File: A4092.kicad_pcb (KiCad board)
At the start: 2 copper layers, 192.7 x 123.3 mm, 102 parts, among them CN1 Zorro3, J1 Conn_02x25_Odd_Even, J2 Conn_01x06_Pin, J3 TO-LED, J4 TO-MB, J5 5787170-5, J6 350543-1, J7 22112042, SW1 219-8MST, U1 SN74ABT16543DGGR, U10 SN74F244DB, U11 SN74ABT16374ADGGR, U12 74LVC07APW_118, U13 SN74ABT16245ADGGR, U14 74ACT521MTCX, U2 SN74ABT16543DGGR, U3 SN74ABT16543DGGR, U4 NCR53c710 SCSI Host Controller, U5 CY74FCT543ATQCT, U6 ATF1508AS-10AU100, U7 SST39SF010, U8 DS21S07A, U9 DS21S07A, Y1 Abracon ACO-50MHz

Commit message: Move IORST to Reset / GCLR Pin
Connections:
- U6 pad 39: IORST -> V5
- U6 pad 89: PLD_FC0 -> IORST
- U6 pad 94: unconnected-(U6-I/O-Pad94) -> PLD_FC0
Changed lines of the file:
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@@
 	(net 332 "unconnected-(U6-I{slash}O{slash}PD1-Pad1)")
 	(net 333 "unconnected-(U6-I{slash}O-Pad100)")
-	(net 334 "unconnected-(U6-I{slash}O-Pad94)")
-	(net 335 "PLD_INTREG")
-	(net 336 "ROM_OE")
-	(net 337 "PLD_CFGLT")
-	(net 338 "ROM_WE")
-	(net 339 "unconnected-(U8-NC-Pad17)")
-	(net 340 "unconnected-(U8-HS-GND-Pad2)")
-	(net 341 "unconnected-(U9-HS-GND-Pad2)")
-	(net 342 "unconnected-(U9-NC-Pad17)")
-	(net 343 "unconnected-(U12-6Y-Pad12)")
-	(net 344 "unconnected-(U12-5Y-Pad10)")
-	(net 345 "SCSI_BUSY")
-	(net 346 "Z_BERR")
-	(net 347 "unconnected-(Y1-NC-Pad1)")
-	(net 348 "unconnected-(RN7-Pad4)")
-	(net 349 "unconnected-(RN7-Pad5)")
-	(net 350 "unconnected-(RN10-Pad5)")
-	(net 351 "unconnected-(RN10-Pad4)")
-	(net 352 "unconnected-(RN16-Pad3)")
-	(net 353 "unconnected-(RN16-Pad6)")
-	(net 354 "unconnected-(U6-I{slash}O-Pad97)")
-	(net 355 "unconnected-(U6-I{slash}O-Pad96)")
+	(net 334 "PLD_INTREG")
+	(net 335 "ROM_OE")
+	(net 336 "PLD_CFGLT")
+	(net 337 "ROM_WE")
+	(net 338 "unconnected-(U8-NC-Pad17)")
+	(net 339 "unconnected-(U8-HS-GND-Pad2)")
+	(net 340 "unconnected-(U9-HS-GND-Pad2)")
+	(net 341 "unconnected-(U9-NC-Pad17)")
+	(net 342 "unconnected-(U12-6Y-Pad12)")
+	(net 343 "unconnected-(U12-5Y-Pad10)")
+	(net 344 "SCSI_BUSY")
+	(net 345 "Z_BERR")
+	(net 346 "unconnected-(Y1-NC-Pad1)")
+	(net 347 "unconnected-(RN7-Pad4)")
+	(net 348 "unconnected-(RN7-Pad5)")
+	(net 349 "unconnected-(RN10-Pad5)")
+	(net 350 "unconnected-(RN10-Pad4)")
+	(net 351 "unconnected-(RN16-Pad3)")
+	(net 352 "unconnected-(RN16-Pad6)")
+	(net 353 "unconnected-(U6-I{slash}O-Pad97)")
+	(net 354 "unconnected-(U6-I{slash}O-Pad96)")
 	(footprint "Capacitor_SMD:C_0603_1608Metric_Pad1.08x0.95mm_HandSolder"
 		(layer "F.Cu")
@@
 			(size 0.9652 1.2446)
 			(layers "F.Cu" "F.Mask" "F.Paste")
-			(net 348 "unconnected-(RN7-Pad4)")
+			(net 347 "unconnected-(RN7-Pad4)")
 			(pintype "passive+no_connect")
 		)
@@
 			(size 0.9652 1.2446)
 			(layers "F.Cu" "F.Mask" "F.Paste")
-			(net 349 "unconnected-(RN7-Pad5)")
+			(net 348 "unconnected-(RN7-Pad5)")
 			(pintype "passive+no_connect")
 		)
@@
 			(size 0.9652 1.2446)
 			(layers "F.Cu" "F.Mask" "F.Paste")
-			(net 351 "unconnected-(RN10-Pad4)")
+			(net 350 "unconnected-(RN10-Pad4)")
 			(pintype "passive+no_connect")
 		)
@@
 			(size 0.9652 1.2446)
 			(layers "F.Cu" "F.Mask" "F.Paste")
-			(net 350 "unconnected-(RN10-Pad5)")
+			(net 349 "unconnected-(RN10-Pad5)")
 			(pintype "passive+no_connect")
 		)
@@
 			(size 0.27 1.4612)
 			(layers "F.Cu" "F.Mask" "F.Paste")
-			(net 199 "IORST")
+			(net 27 "V5")
 			(pinfunction "VCCINT")
 			(pintype "power_in")
@@
 			(size 0.27 1.4612)
 			(layers "F.Cu" "F.Mask" "F.Paste")
-			(net 336 "ROM_OE")
+			(net 335 "ROM_OE")
 			(pinfunction "I/O")
 			(pintype "bidirectional")
@@
 			(size 0.27 1.4612)
 			(layers "F.Cu" "F.Mask" "F.Paste")
-			(net 337 "PLD_CFGLT")
+			(net 336 "PLD_CFGLT")
 			(pinfunction "I/O")
 			(pintype "bidirectional")
@@
 			(size 0.27 1.4612)
 			(layers "F.Cu" "F.Mask" "F.Paste")
-			(net 335 "PLD_INTREG")
+			(net 334 "PLD_INTREG")
 			(pinfunction "I/O")
 			(pintype "bidirectional")
@@
 			(size 0.27 1.4612)
 			(layers "F.Cu" "F.Mask" "F.Paste")
-			(net 211 "PLD_FC0")
+			(net 199 "IORST")
 			(pinfunction "INPUT/GCLR")
 			(pintype "bidirectional")
@@
 			(size 0.27 1.4612)
 			(layers "F.Cu" "F.Mask" "F.Paste")
-			(net 334 "unconnected-(U6-I{slash}O-Pad94)")
+			(net 211 "PLD_FC0")
 			(pinfunction "I/O")
 			(pintype "bidirectional")
@@
 			(size 0.27 1.4612)
 			(layers "F.Cu" "F.Mask" "F.Paste")
-			(net 355 "unconnected-(U6-I{slash}O-Pad96)")
+			(net 354 "unconnected-(U6-I{slash}O-Pad96)")
 			(pinfunction "I/O")
 			(pintype "bidirectional")
@@
 			(size 0.27 1.4612)
 			(layers "F.Cu" "F.Mask" "F.Paste")
-			(net 354 "unconnected-(U6-I{slash}O-Pad97)")
+			(net 353 "unconnected-(U6-I{slash}O-Pad97)")
 			(pinfunction "I/O")
 			(pintype "bidirectional")
@@
 			(layers "F.Cu" "F.Mask" "F.Paste")
 			(roundrect_rratio 0.25)
-			(net 341 "unconnected-(U9-HS-GND-Pad2)")
+			(net 340 "unconnected-(U9-HS-GND-Pad2)")
 			(pinfunction "HS-GND")
 			(pintype "power_in")
@@
 			(layers "F.Cu" "F.Mask" "F.Paste")
 			(roundrect_rratio 0.25)
-			(net 342 "unconnected-(U9-NC-Pad17)")
+			(net 341 "unconnected-(U9-NC-Pad17)")
 			(pinfunction "NC")
 			(pintype "no_connect")
@@
 			(size 0.9652 0.6604)
 			(layers "F.Cu" "F.Mask" "F.Paste")
-			(net 352 "unconnected-(RN16-Pad3)")
+			(net 351 "unconnected-(RN16-Pad3)")
 			(pintype "passive+no_connect")
 		)
@@
 			(size 0.9652 0.6604)
 			(layers "F.Cu" "F.Mask" "F.Paste")
-			(net 353 "unconnected-(RN16-Pad6)")
+			(net 352 "unconnected-(RN16-Pad6)")
 			(pintype "passive+no_connect")
 		)
@@
 			(size 1.6764 0.2794)
 			(layers "F.Cu" "F.Mask" "F.Paste")
-			(net 335 "PLD_INTREG")
+			(net 334 "PLD_INTREG")
 			(pinfunction "2CLK")
 			(pintype "input")
@@
 			(size 1.6764 0.2794)
 			(layers "F.Cu" "F.Mask" "F.Paste")
-			(net 337 "PLD_CFGLT")
+			(net 336 "PLD_CFGLT")
 			(pinfunction "1CLK")
 			(pintype "input")
@@
 			(layers "F.Cu" "F.Mask" "F.Paste")
 			(roundrect_rratio 0.25)
-			(net 340 "unconnected-(U8-HS-GND-Pad2)")
+			(net 339 "unconnected-(U8-HS-GND-Pad2)")
 			(pinfunction "HS-GND")
 			(pintype "power_in")
@@
 			(layers "F.Cu" "F.Mask" "F.Paste")
 			(roundrect_rratio 0.25)
-			(net 339 "unconnected-(U8-NC-Pad17)")
+			(net 338 "unconnected-(U8-NC-Pad17)")
 			(pinfunction "NC")
 			(pintype "no_connect")
@@
 			(layers "*.Cu" "*.Mask")
 			(remove_unused_layers no)
-			(net 347 "unconnected-(Y1-NC-Pad1)")
+			(net 346 "unconnected-(Y1-NC-Pad1)")
 			(pinfunction "NC")
 			(pintype "no_connect")
@@
 			(size 1.4605 0.3556)
 			(layers "F.Cu" "F.Mask" "F.Paste")
-			(net 345 "SCSI_BUSY")
+			(net 344 "SCSI_BUSY")
 			(pinfunction "1A")
 			(pintype "input")
@@
 			(size 1.4605 0.3556)
 			(layers "F.Cu" "F.Mask" "F.Paste")
-			(net 345 "SCSI_BUSY")
+			(net 344 "SCSI_BUSY")
 			(pinfunction "2A")
 			(pintype "input")
@@
 			(size 1.4605 0.3556)
 			(layers "F.Cu" "F.Mask" "F.Paste")
-			(net 346 "Z_BERR")
+			(net 345 "Z_BERR")
 			(pinfunction "3A")
 			(pintype "input")
@@
 			(size 1.4605 0.3556)
 			(layers "F.Cu" "F.Mask" "F.Paste")
-			(net 344 "unconnected-(U12-5Y-Pad10)")
+			(net 343 "unconnected-(U12-5Y-Pad10)")
 			(pinfunction "5Y")
 			(pintype "output+no_connect")
@@
 			(size 1.4605 0.3556)
 			(layers "F.Cu" "F.Mask" "F.Paste")
-			(net 343 "unconnected-(U12-6Y-Pad12)")
+			(net 342 "unconnected-(U12-6Y-Pad12)")
 			(pinfunction "6Y")
 			(pintype "output+no_connect")
@@
 			(layers "F.Cu" "F.Mask" "F.Paste")
 			(roundrect_rratio 0.25)
-			(net 338 "ROM_WE")
+			(net 337 "ROM_WE")
 			(pinfunction "PGM")
 			(pintype "input")
@@
 			(layers "F.Cu" "F.Mask" "F.Paste")
 			(roundrect_rratio 0.25)
-			(net 336 "ROM_OE")
+			(net 335 "ROM_OE")
 			(pinfunction "OE")
 			(pintype "input")

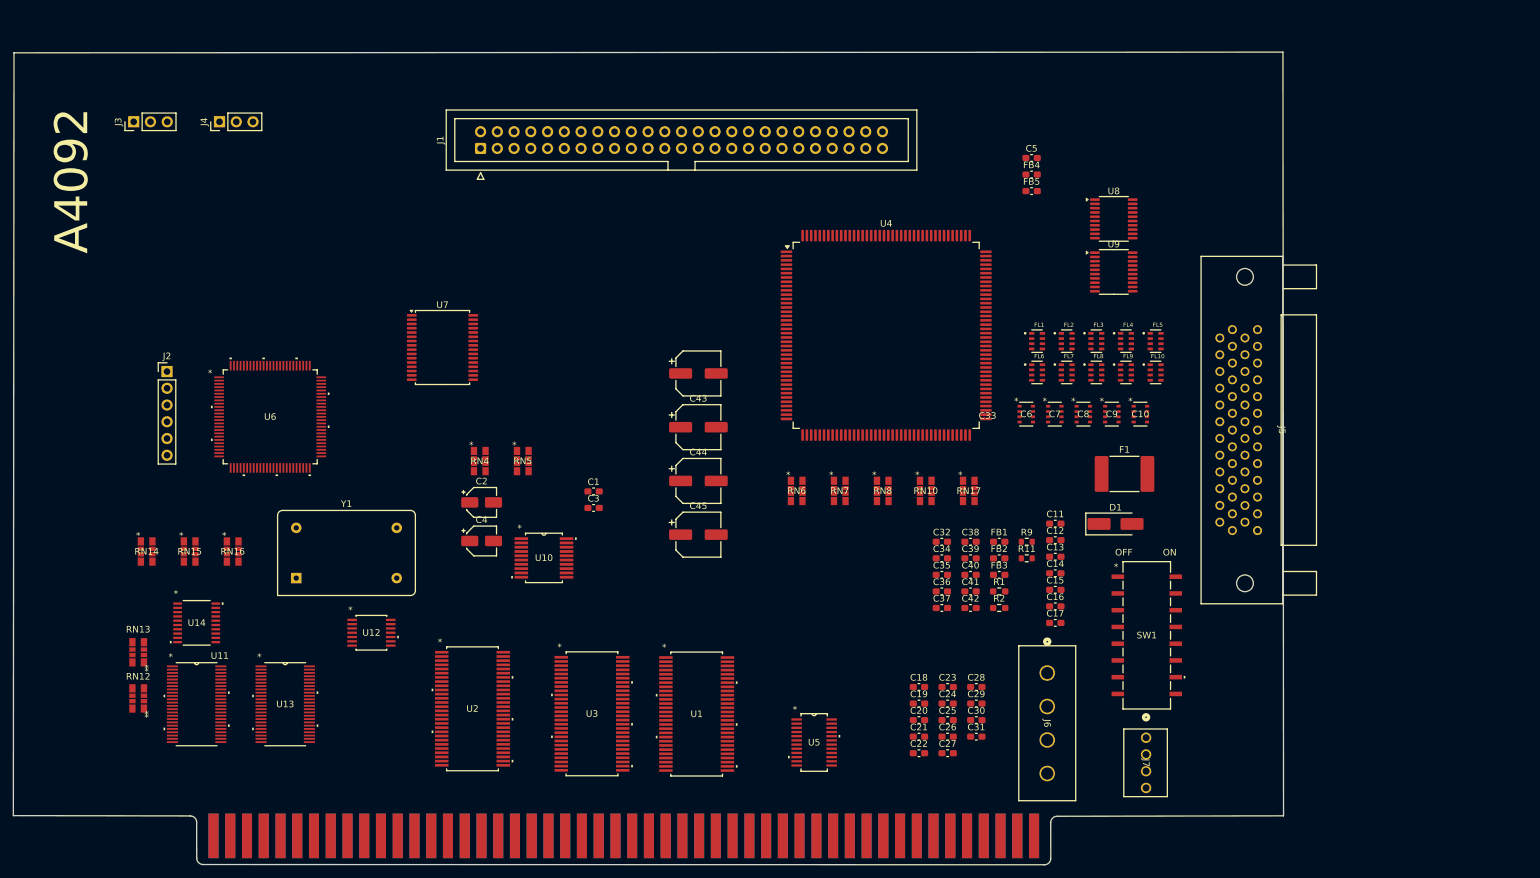
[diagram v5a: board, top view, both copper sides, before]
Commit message: Free up some pins and add an LED
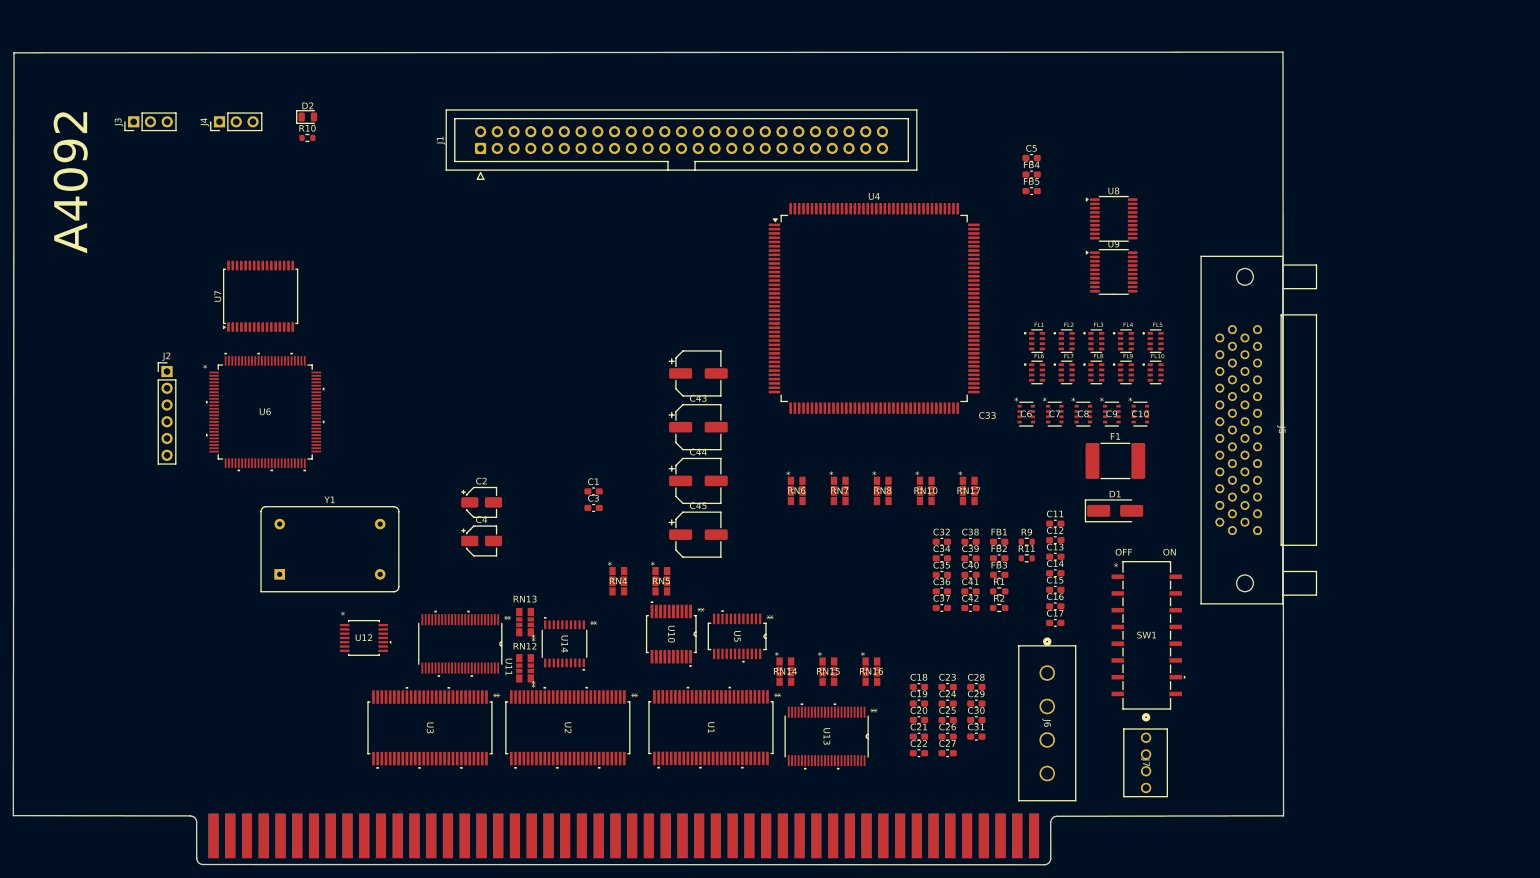
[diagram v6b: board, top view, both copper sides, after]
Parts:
- added D2: LED (green), LED_SMD:LED_0805_2012Metric, F.Cu at (76.9, 43.3)
- added R10: 2.2k, Resistor_SMD:R_0603_1608Metric, F.Cu at (76.8, 46.5)
- moved RN14 98.6 mm to (149.3, 127.4)
- moved RN16 98.6 mm to (162.3, 127.4)
- moved RN15 98.6 mm to (155.8, 127.4)
- moved U13 82.3 mm to (155.6, 137.2), turned to -90 degrees
- moved RN12 58.9 mm to (109.8, 126.9)
- moved RN13 58.9 mm to (109.8, 119.9)
- moved U14 55.9 mm to (115.8, 123.2), turned to -90 degrees
- moved U11 41.0 mm to (100.0, 123.2), turned to -90 degrees
- moved U7 28.7 mm to (69.7, 70.5), turned to 90 degrees
- moved RN5 27.8 mm to (130.5, 113.7)
- moved RN4 27.8 mm to (123.9, 113.7)
- moved U3 24.7 mm to (95.4, 135.9), turned to -90 degrees
- moved U10 22.5 mm to (132.0, 121.7), turned to -90 degrees
- moved U5 19.9 mm to (142.0, 122.1), turned to -90 degrees
- moved U2 14.7 mm to (116.3, 135.9), turned to -90 degrees
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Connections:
- U6 pad 25: PLD_NOZ3 -> PLD_READ
- U6 pad 27: PLD_READ -> PLD_SIZ0
- U6 pad 28: PLD_SCSI -> PLD_SIZ1
- U6 pad 29: PLD_SIZ0 -> PLD_AS
- U6 pad 30: PLD_SIZ1 -> PLD_DS
- U6 pad 31: PLD_AS -> PLD_FC0
- U6 pad 32: PLD_DS -> PLD_FC1
- U6 pad 33: PLD_MYBUS -> PLD_FC2
- U6 pad 58: PLD_INTSPC -> Z_MTACK
- U6 pad 75: PLD_FC2 -> CLK
- U6 pad 76: CLK -> CBREQ
- U6 pad 77: CBREQ -> BERR
- U6 pad 78: BERR -> Z_BGn
- U6 pad 79: PLD_ASQ -> Z_BRn
- U6 pad 88: PLD_FC1 -> unconnected-(U6-INPUT/OE1-Pad88)
- U6 pad 90: Z_MTACK -> unconnected-(U6-INPUT/OE2/GCLK2-Pad90)
- U6 pad 92: Z_BGn -> unconnected-(U6-I/O-Pad92)
- U6 pad 93: Z_BRn -> unconnected-(U6-I/O-Pad93)
- U6 pad 94: PLD_FC0 -> unconnected-(U6-I/O-Pad94)

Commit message: Move to XC95144XL
and other changes related to that.
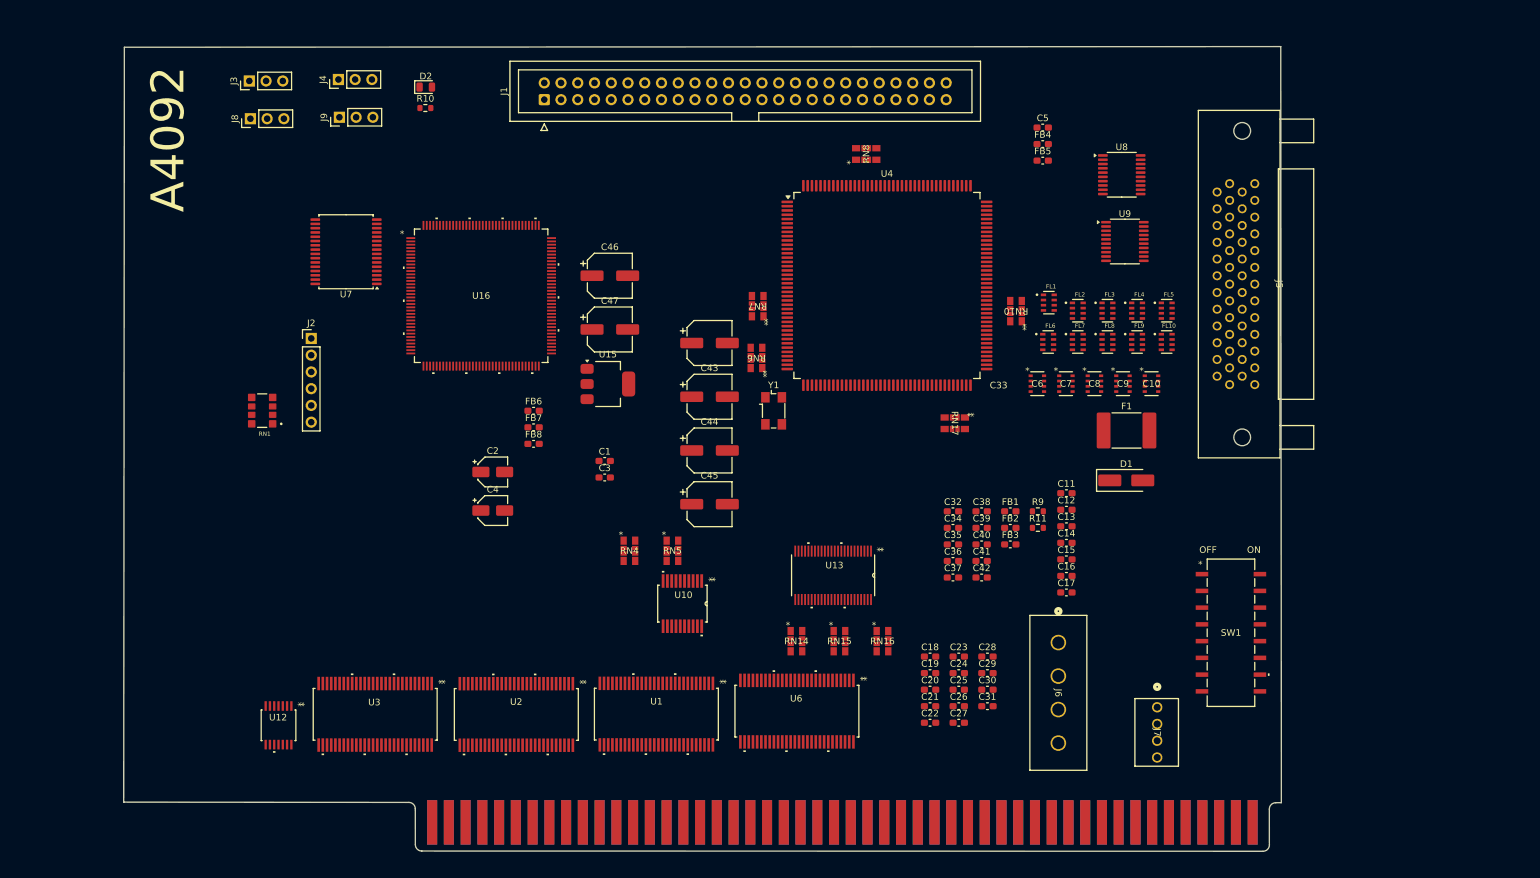
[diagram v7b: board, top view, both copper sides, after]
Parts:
- removed R1, R2: 22, Resistor_SMD:R_0603_1608Metric_Pad0.98x0.95mm_HandSolder
- removed RN12, RN13: 1K, CAY16_102J4LF:BO_CAY16
- removed U11: SN74ABT16374ADGGR, SN74ABT16374ADGGR:DGG48
- removed U14: 74ACT521MTCX, 74ACT521MTCX:TSSOP20_4P4X6P5_ONS
- removed U5: CY74FCT543ATQCT, CY74FCT543ATQCT:DBQ24
- added C46: 10uF, Capacitor_SMD:CP_Elec_6.3x7.7, F.Cu at (122.7, 67.3)
- added C47: 22uF, Capacitor_SMD:CP_Elec_6.3x7.7, F.Cu at (122.7, 75.5)
- added FB6: 60, Capacitor_SMD:C_0603_1608Metric_Pad1.08x0.95mm_HandSolder, F.Cu at (111.1, 87.8)
- added FB7: 60, Capacitor_SMD:C_0603_1608Metric_Pad1.08x0.95mm_HandSolder, F.Cu at (111.1, 90.3)
- added FB8: 60, Capacitor_SMD:C_0603_1608Metric_Pad1.08x0.95mm_HandSolder, F.Cu at (111.1, 92.8)
- added J8: TO-A3000-LED, Connector_PinHeader_2.54mm:PinHeader_1x03_P2.54mm_Vertical, F.Cu at (68.1, 43.5)
- added J9: TO-A3000-MB, Connector_PinHeader_2.54mm:PinHeader_1x03_P2.54mm_Vertical, F.Cu at (81.6, 43.3)
- added RN1: 4.7K, YC324-FK-071KL:RESCAXS127P508X320X70-8N, F.Cu at (69.9, 87.8)
- added U15: AMS1117-3.3, Package_TO_SOT_SMD:SOT-223-3_TabPin2, F.Cu at (122.4, 83.8)
- added U16: XC95144XL-TQ144, XC95144XL_5TQG144C:144-TQFP_XIL, F.Cu at (103.1, 70.4)
- U6: value ATF1508AS-10AU100 -> SN74ABT16543DGGR; footprint ATF1508AS:100A_ATM -> 74FCT16543:DL56
- Y1: footprint Oscillator:Oscillator_DIP-14 -> Oscillator:Oscillator_SMD_Fox_FT5H_5.0x3.2mm
- moved U6 92.5 mm to (151.0, 133.4), turned to -90 degrees
- moved Y1 78.9 mm to (147.5, 87.8)
- moved RN8 51.2 mm to (161.6, 48.9), turned to 90 degrees
- moved CN1 33.2 mm to (95.7, 150.3)
- moved RN7 30.7 mm to (145.1, 72.0), turned to 180 degrees
- moved RN10 30.5 mm to (184.3, 72.7), turned to 180 degrees
- moved U13 24.5 mm to (156.5, 112.8)
- moved J2 22.4 mm to (77.4, 76.9)
- moved J5 22.1 mm to (220.5, 53.4)
- moved RN6 21.1 mm to (144.9, 79.8), turned to 180 degrees
- moved J4 19.1 mm to (81.5, 37.6)
- moved J3 18.6 mm to (68.0, 37.8)
- moved U12 18.5 mm to (72.4, 135.5), turned to -90 degrees
- moved R10 18.5 mm to (94.7, 41.9)
- moved D2 18.5 mm to (94.7, 38.7)
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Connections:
- J2 pad 6: V5 -> V3_3
- U6 pad 1: unconnected-(U6-I/O/PD1-Pad1) -> IORST
- U6 pad 10: A5 -> A11
- U6 pad 12: A6 -> A10
- U6 pad 13: A8 -> A9
- U6 pad 14: A17 -> A8
- U6 pad 15: TMS -> unconnected-(U6-2A1-Pad15)
- U6 pad 16: A18 -> unconnected-(U6-2A2-Pad16)
- U6 pad 17: A19 -> unconnected-(U6-2A3-Pad17)
- U6 pad 18: V5 -> GND
- U6 pad 19: A23 -> unconnected-(U6-2A4-Pad19)
- U6 pad 2: unconnected-(U6-I/O/PD1-Pad2) -> GND
- U6 pad 20: PLD_DS0 -> unconnected-(U6-2A5-Pad20)
- U6 pad 21: PLD_DS1 -> unconnected-(U6-2A6-Pad21)
- U6 pad 22: PLD_DS2 -> V5
- U6 pad 23: PLD_DS3 -> unconnected-(U6-2A7-Pad23)
- U6 pad 24: PLD_DOE -> unconnected-(U6-2A8-Pad24)
- U6 pad 25: PLD_READ -> GND
- U6 pad 27: PLD_SIZ0 -> GND
- U6 pad 28: PLD_SIZ1 -> GND
- U6 pad 29: PLD_AS -> GND
- U6 pad 3: V5 -> MASTER
- U6 pad 30: PLD_DS -> GND
- U6 pad 31: PLD_FC0 -> GND
- U6 pad 32: PLD_FC1 -> GND
- U6 pad 33: PLD_FC2 -> unconnected-(U6-2B8-Pad33)
- U6 pad 34: V5 -> unconnected-(U6-2B7-Pad34)
- U6 pad 35: STERM -> V5
- U6 pad 36: SREG -> unconnected-(U6-2B6-Pad36)
- U6 pad 37: Z_CINH -> unconnected-(U6-2B5-Pad37)
- U6 pad 38: GND -> unconnected-(U6-2B4-Pad38)
- U6 pad 39: V5 -> GND
- U6 pad 4: TDI -> GND
- U6 pad 40: NCR_INT -> unconnected-(U6-2B3-Pad40)
- U6 pad 41: Z_SENSEZ3 -> unconnected-(U6-2B2-Pad41)
- U6 pad 42: PLD_FCS -> unconnected-(U6-2B1-Pad42)
- U6 pad 43: GND -> Z_A8D0
- U6 pad 44: Z_SLAVE -> Z_A9D1
- U6 pad 45: Z_CFGOUT -> Z_A10D2
- U6 pad 46: Z_CFGIN -> GND
- U6 pad 47: ROM_OE -> Z_A11D3
- U6 pad 48: PLD_NACK -> Z_A12D4
- U6 pad 49: PLD_INT -> Z_A13D5
- U6 pad 5: A0 -> A15
- U6 pad 50: Z_INT2 -> V5
- U6 pad 51: V5 -> Z_A14D6
- U6 pad 52: PLD_CFGLT -> Z_A15D7
- U6 pad 53: PLD_MTCR -> GND
- U6 pad 54: SLACK -> BMASTER
- U6 pad 55: MATCH -> PLD_FCS
- U6 pad 56: PLD_INTREG -> ABOEH
- U6 pad 6: A1 -> A14
- U6 pad 7: A2 -> V5
- U6 pad 8: A3 -> A13
- U6 pad 9: A4 -> A12
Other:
- board size 192.7 x 123.3 mm -> 175.6 x 122.1 mm
